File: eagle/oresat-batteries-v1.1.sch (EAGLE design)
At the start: 62 parts, among them IC1 74AHC1G08DBV, U1 TCAN330, U2 STM32F042K6, X1 16MHz

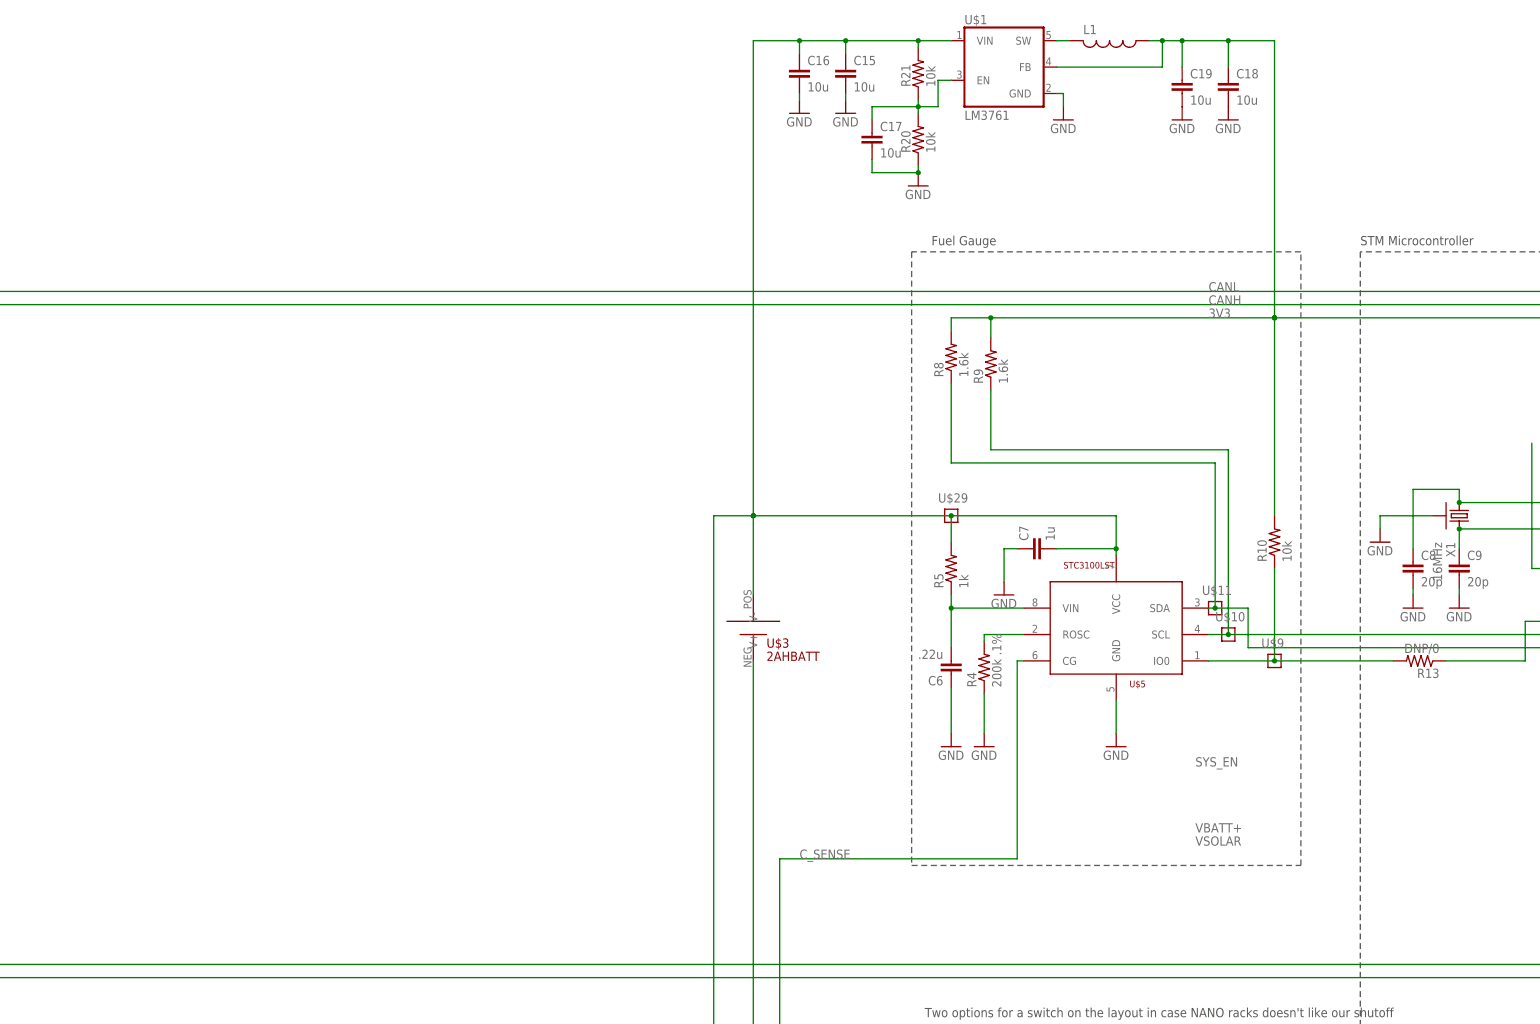
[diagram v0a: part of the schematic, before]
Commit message: Added ideal diodes and new fuel gauge
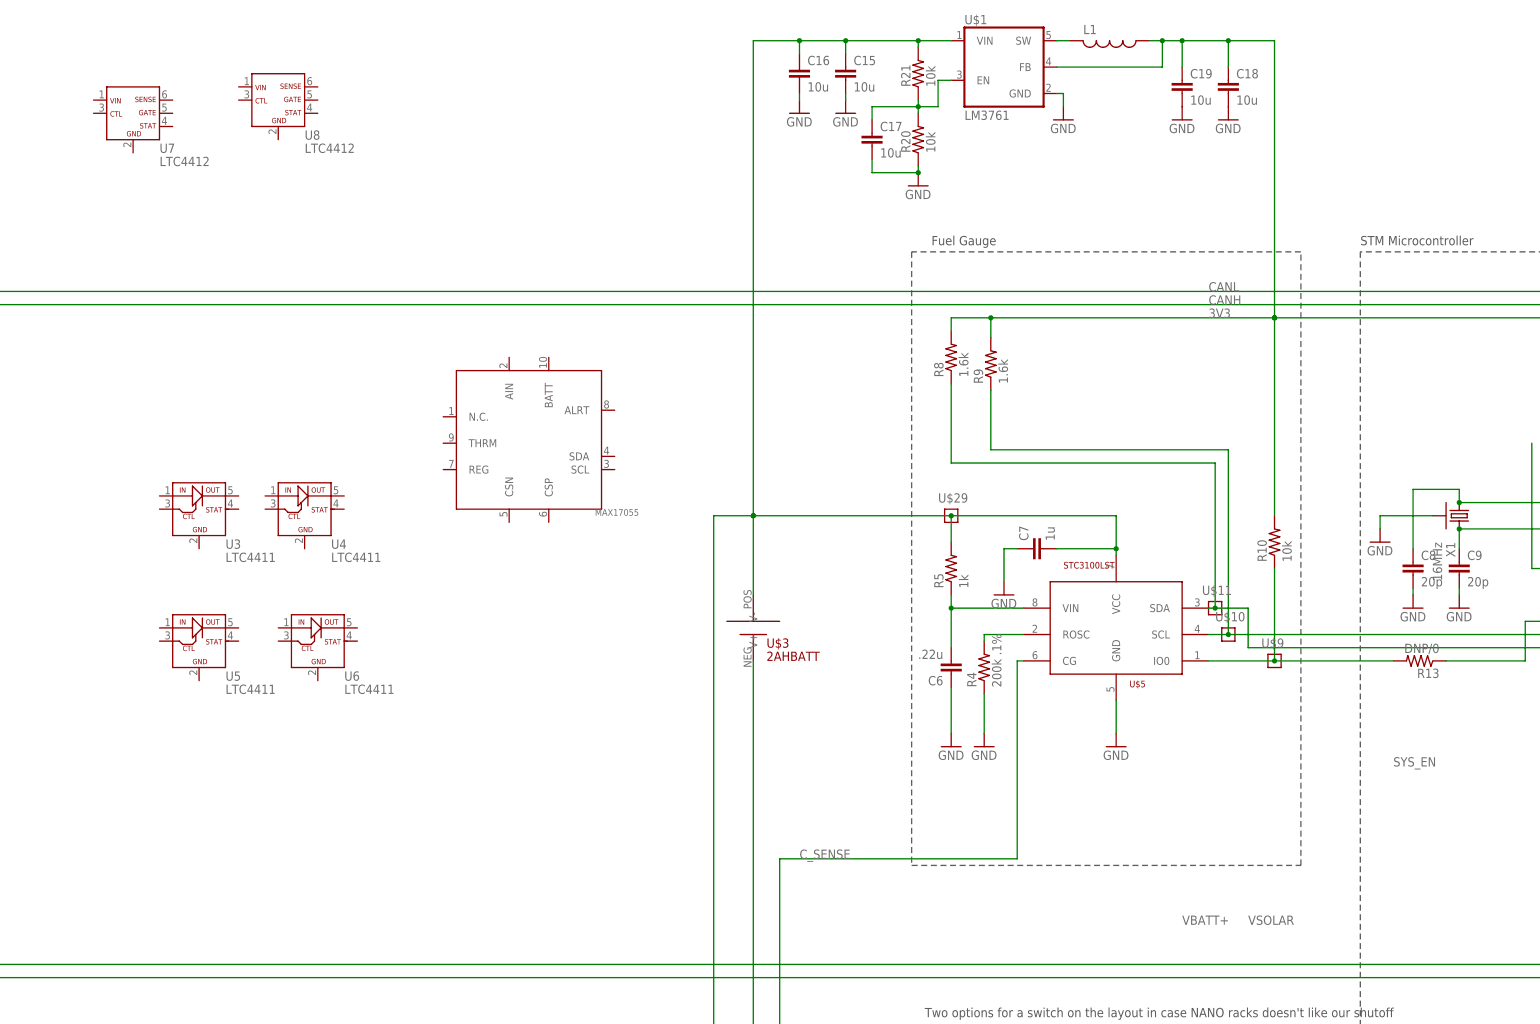
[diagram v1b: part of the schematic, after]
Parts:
- added U$6: MAX17055, max17055:MAX17055
- added U3, U4, U5, U6: LTC4411, ltc4411:LTC4411
- added U7, U8: LTC4412, ltc4412:LTC4412
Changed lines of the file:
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@@
 <setting verticaltext="up"/>
 </settings>
-<grid distance="1.27" unitdist="mm" unit="mm" style="lines" multiple="1" display="no" altdistance="0.01" altunitdist="inch" altunit="inch"/>
+<grid distance="0.1" unitdist="inch" unit="inch" style="lines" multiple="1" display="no" altdistance="0.01" altunitdist="inch" altunit="inch"/>
 <layers>
 <layer number="1" name="Top" color="4" fill="1" visible="no" active="no"/>
@@
 <part name="GND41" library="supply1" deviceset="GND" device=""/>
 <part name="L1" library="rcl" deviceset="L-US" device="L2012C"/>
+<part name="U3" library="ltc4411" deviceset="LTC4411" device=""/>
+<part name="U4" library="ltc4411" deviceset="LTC4411" device=""/>
+<part name="U5" library="ltc4411" deviceset="LTC4411" device=""/>
+<part name="U6" library="ltc4411" deviceset="LTC4411" device=""/>
+<part name="U7" library="ltc4412" deviceset="LTC4412" device=""/>
+<part name="U8" library="ltc4412" deviceset="LTC4412" device=""/>
+<part name="U$6" library="max17055" deviceset="MAX17055" device=""/>
 </parts>
 <sheets>
@@
 <instance part="GND41" gate="1" x="297.18" y="326.39"/>
 <instance part="L1" gate="G$1" x="274.32" y="341.63" rot="R270"/>
+<instance part="U3" gate="G$1" x="99.06" y="251.46"/>
+<instance part="U4" gate="G$1" x="119.38" y="251.46"/>
+<instance part="U5" gate="G$1" x="99.06" y="226.06"/>
+<instance part="U6" gate="G$1" x="121.92" y="226.06"/>
+<instance part="U7" gate="G$1" x="86.36" y="327.66"/>
+<instance part="U8" gate="G$1" x="114.3" y="330.2"/>
+<instance part="U$6" gate="G$1" x="162.56" y="264.16"/>
 </instances>
 <busses>
@@
 <junction x="510.54" y="161.29"/>
 <wire x1="45.72" y1="161.29" x2="510.54" y2="161.29" width="0.1524" layer="91"/>
-<label x="290.83" y="186.69" size="1.778" layer="95"/>
+<label x="300.99" y="171.45" size="1.778" layer="95"/>
 <pinref part="CF1" gate="G$1" pin="4"/>
 <wire x1="45.72" y1="285.75" x2="25.4" y2="285.75" width="0.3048" layer="91"/>
@@
 <wire x1="457.2" y1="189.23" x2="457.2" y2="163.83" width="0.1524" layer="91"/>
 <wire x1="457.2" y1="163.83" x2="48.26" y2="163.83" width="0.1524" layer="91"/>
-<label x="290.83" y="189.23" size="1.778" layer="95"/>
+<label x="288.29" y="171.45" size="1.778" layer="95"/>
 <label x="505.46" y="189.23" size="1.778" layer="95" rot="MR0"/>
 </segment>
@@
 <wire x1="383.54" y1="240.03" x2="355.6" y2="240.03" width="0.1524" layer="91"/>
 <wire x1="355.6" y1="240.03" x2="355.6" y2="264.16" width="0.1524" layer="91"/>
-<label x="290.83" y="201.93" size="1.778" layer="95"/>
-</segment>
-</net>
+<label x="328.93" y="201.93" size="1.778" layer="95"/>
+</segment>
+</net>

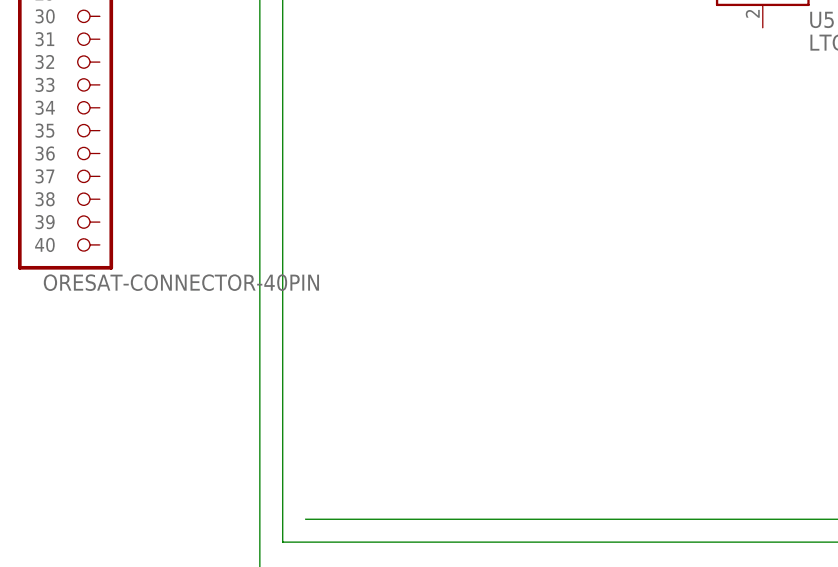
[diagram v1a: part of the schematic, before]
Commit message: Updated batteries with latest OreSat card and connector.
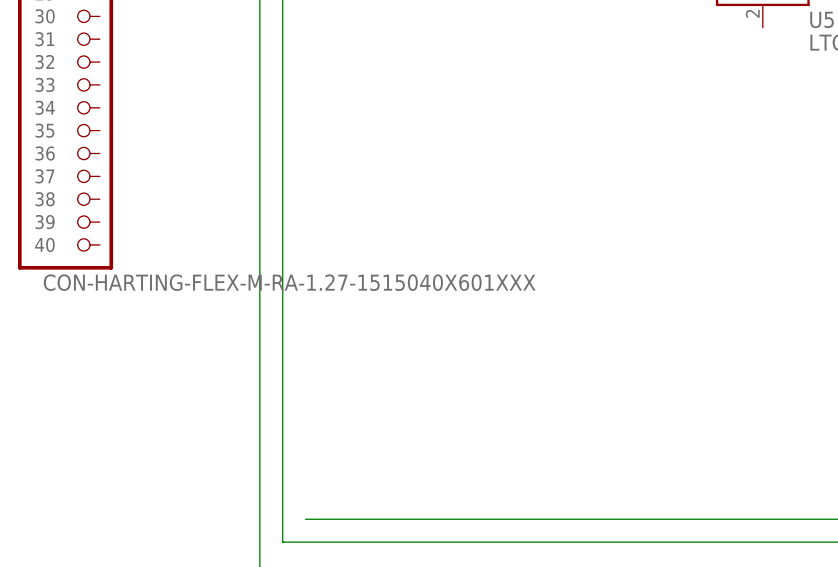
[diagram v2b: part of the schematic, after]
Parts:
- CF1: value ORESAT-CONNECTOR-40PIN -> CON-HARTING-FLEX-M-RA-1.27-1515040X601XXX; device low-gain-radio:ORESAT-CONNECTOR-40PIN -> oresat-eagle:CON-HARTING-FLEX-M-RA-1.27-1515040X601XXX
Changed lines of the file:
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@@
 <?xml version="1.0" encoding="utf-8"?>
 <!DOCTYPE eagle SYSTEM "eagle.dtd">
-<eagle version="7.5.0">
+<eagle version="7.7.0">
 <drawing>
 <settings>
@@
 <layer number="2" name="Route2" color="1" fill="3" visible="no" active="no"/>
 <layer number="3" name="Route3" color="4" fill="3" visible="no" active="no"/>
+<layer number="4" name="Route4" color="1" fill="4" visible="no" active="no"/>
+<layer number="5" name="Route5" color="4" fill="4" visible="no" active="no"/>
+<layer number="6" name="Route6" color="1" fill="8" visible="no" active="no"/>
+<layer number="7" name="Route7" color="4" fill="8" visible="no" active="no"/>
+<layer number="8" name="Route8" color="1" fill="2" visible="no" active="no"/>
+<layer number="9" name="Route9" color="4" fill="2" visible="no" active="no"/>
+<layer number="10" name="Route10" color="1" fill="7" visible="no" active="no"/>
+<layer number="11" name="Route11" color="4" fill="7" visible="no" active="no"/>
+<layer number="12" name="Route12" color="1" fill="5" visible="no" active="no"/>
+<layer number="13" name="Route13" color="4" fill="5" visible="no" active="no"/>
 <layer number="14" name="Route14" color="1" fill="6" visible="no" active="no"/>
 <layer number="15" name="Route15" color="4" fill="6" visible="no" active="no"/>
@@
 <part name="U$2" library="oresat-batteries" deviceset="BQ2970" device=""/>
 <part name="U1" library="oresat-batteries" deviceset="TCAN330" device=""/>
-<part name="CF1" library="low-gain-radio" deviceset="ORESAT-CONNECTOR-40PIN" device=""/>
+<part name="CF1" library="oresat-eagle" deviceset="CON-HARTING-FLEX-M-RA-1.27-1515040X601XXX" device=""/>
 <part name="U$5" library="oresat-batteries" deviceset="STC3100LST" device=""/>
 <part name="C1" library="rcl" deviceset="C-EU" device="C0603" value=".1u"/>
